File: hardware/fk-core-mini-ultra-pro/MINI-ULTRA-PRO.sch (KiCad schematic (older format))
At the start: 70 parts, among them J1 S2B-PH-SM4-TB, J2 MICRO-USB, J3 RF-SMA-EDGE, J4 CONN-HDR-1x19, J5 CONN-HDR-1x19, J6 CONN-HDR-2x5, J7 RF-SMA-EDGE, M1 MOUNT_HOLE, M2 MOUNT_HOLE, M3 MOUNT_HOLE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

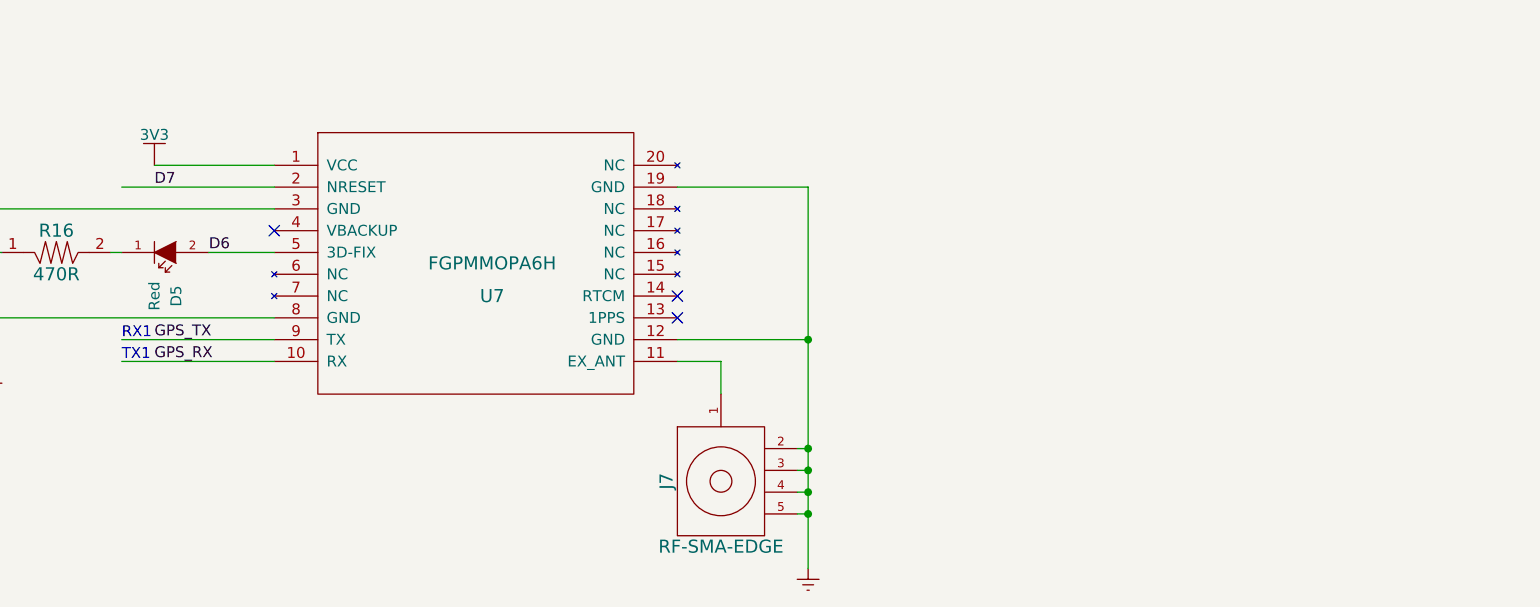
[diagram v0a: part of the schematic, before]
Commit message: Laying out our additions to the MUP pcb. SD/GPS/Fuel gauge.
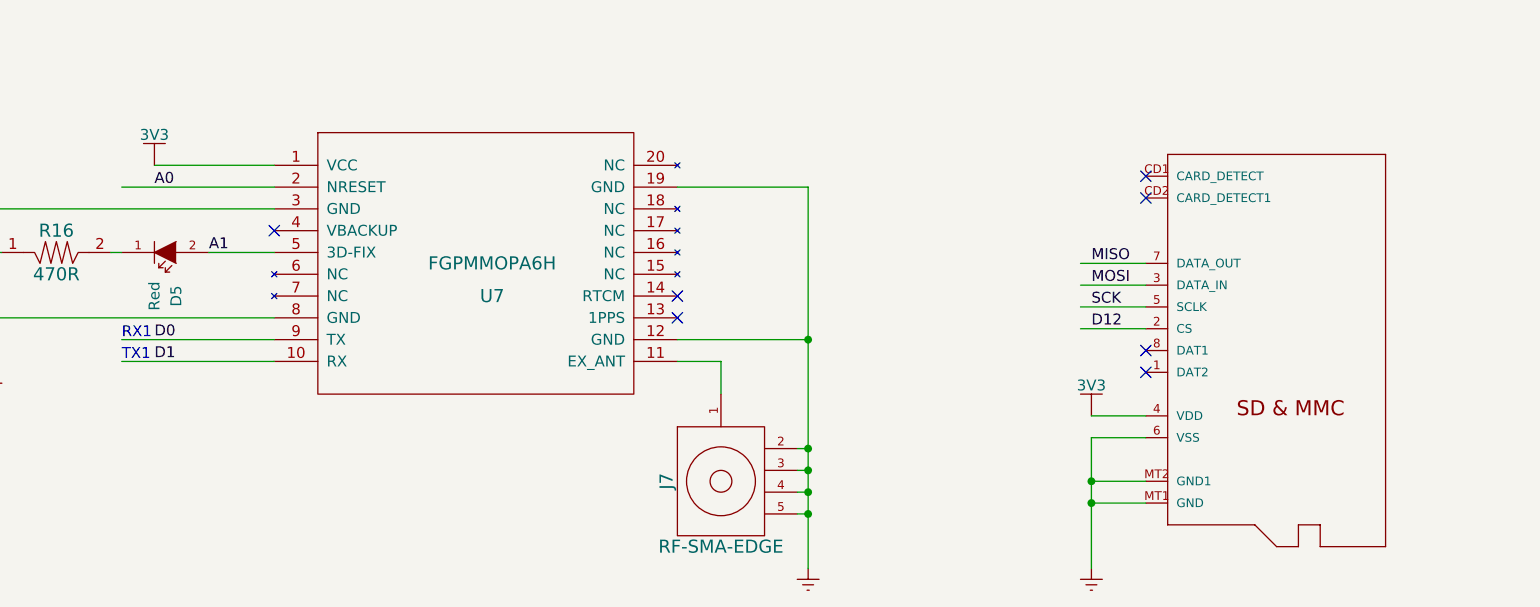
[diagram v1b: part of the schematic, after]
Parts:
- added M7: MICROSD, microsd:MICROSD, symbol MICROSD
- U7: footprint (none) -> FGPMMOPA6H:FGPMMOPA6H
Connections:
- net labels removed: GPS_RX, GPS_TX
- wire segments 317 -> 326
- no-connect marks 21 -> 25
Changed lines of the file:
@@
 F 0 "U7" H 8450 12350 60  0000 C CNN
 F 1 "FGPMMOPA6H" H 8450 12500 60  0000 C CNN
-F 2 "" H 8450 12500 60  0001 C CNN
+F 2 "FGPMMOPA6H:FGPMMOPA6H" H 8450 12500 60  0001 C CNN
 F 3 "" H 8450 12500 60  0001 C CNN
 	1    8450 12500
@@
 Connection ~ 6150 12450
 Text Label 6900 12150 0    50   ~ 0
-D7
+A0
 Text Label 6900 12850 0    50   ~ 0
-GPS_TX
+D0
 Text Label 6900 12950 0    50   ~ 0
-GPS_RX
+D1
 Text Label 7150 12450 0    50   ~ 0
-D6
+A1
 Text Notes 6750 12950 0    50   ~ 0
 TX1
 Text Notes 6750 12850 0    50   ~ 0
 RX1
+$Comp
+L MICROSD M7
+U 1 1 58837EB0
+P 12150 12800
+F 0 "M7" H 12150 12800 45  0001 C CNN
+F 1 "MICROSD" H 12150 12800 45  0001 C CNN
+F 2 "microsd:MICROSD" H 12180 12950 20  0001 C CNN
+F 3 "" H 12150 12800 60  0001 C CNN
+	1    12150 12800
+	1    0    0    -1
+$EndComp
+NoConn ~ 11450 12100
+NoConn ~ 11450 12200
+$Comp
+L GND #PWR070
+U 1 1 58838941
+P 11200 13900
+F 0 "#PWR070" H 11200 13650 50  0001 C CNN
+F 1 "GND" H 11200 13750 50  0001 C CNN
+F 2 "" H 11200 13900 60  0000 C CNN
+F 3 "" H 11200 13900 60  0000 C CNN
+	1    11200 13900
+	1    0    0    -1
+$EndComp
+Wire Wire Line
+	11450 13500 11200 13500
+Wire Wire Line
+	11200 13300 11200 13900
+Wire Wire Line
+	11450 13600 11200 13600
+Connection ~ 11200 13600
+Wire Wire Line
+	11450 13300 11200 13300
+Connection ~ 11200 13500
+$Comp
+L 3V3 #PWR071
+U 1 1 58839315
+P 11200 13200
+F 0 "#PWR071" H 11200 13050 50  0001 C CNN
+F 1 "3V3" H 11200 13340 50  0000 C CNN
+F 2 "" H 11200 13200 60  0000 C CNN
+F 3 "" H 11200 13200 60  0000 C CNN
+	1    11200 13200
+	1    0    0    -1
+$EndComp
+Wire Wire Line
+	11450 13200 11200 13200
+NoConn ~ 11450 12900
+NoConn ~ 11450 13000
+Text Label 11200 12600 0    50   ~ 0
+MOSI
+Text Label 11200 12500 0    50   ~ 0
+MISO
+Text Label 11200 12700 0    50   ~ 0
+SCK
+Wire Wire Line
+	11450 12700 11150 12700
+Wire Wire Line
+	11150 12600 11450 12600
+Wire Wire Line
+	11150 12500 11450 12500
+Wire Wire Line
+	11150 12800 11450 12800
+Text Label 11200 12800 0    50   ~ 0
+D12
 $EndSCHEMATC

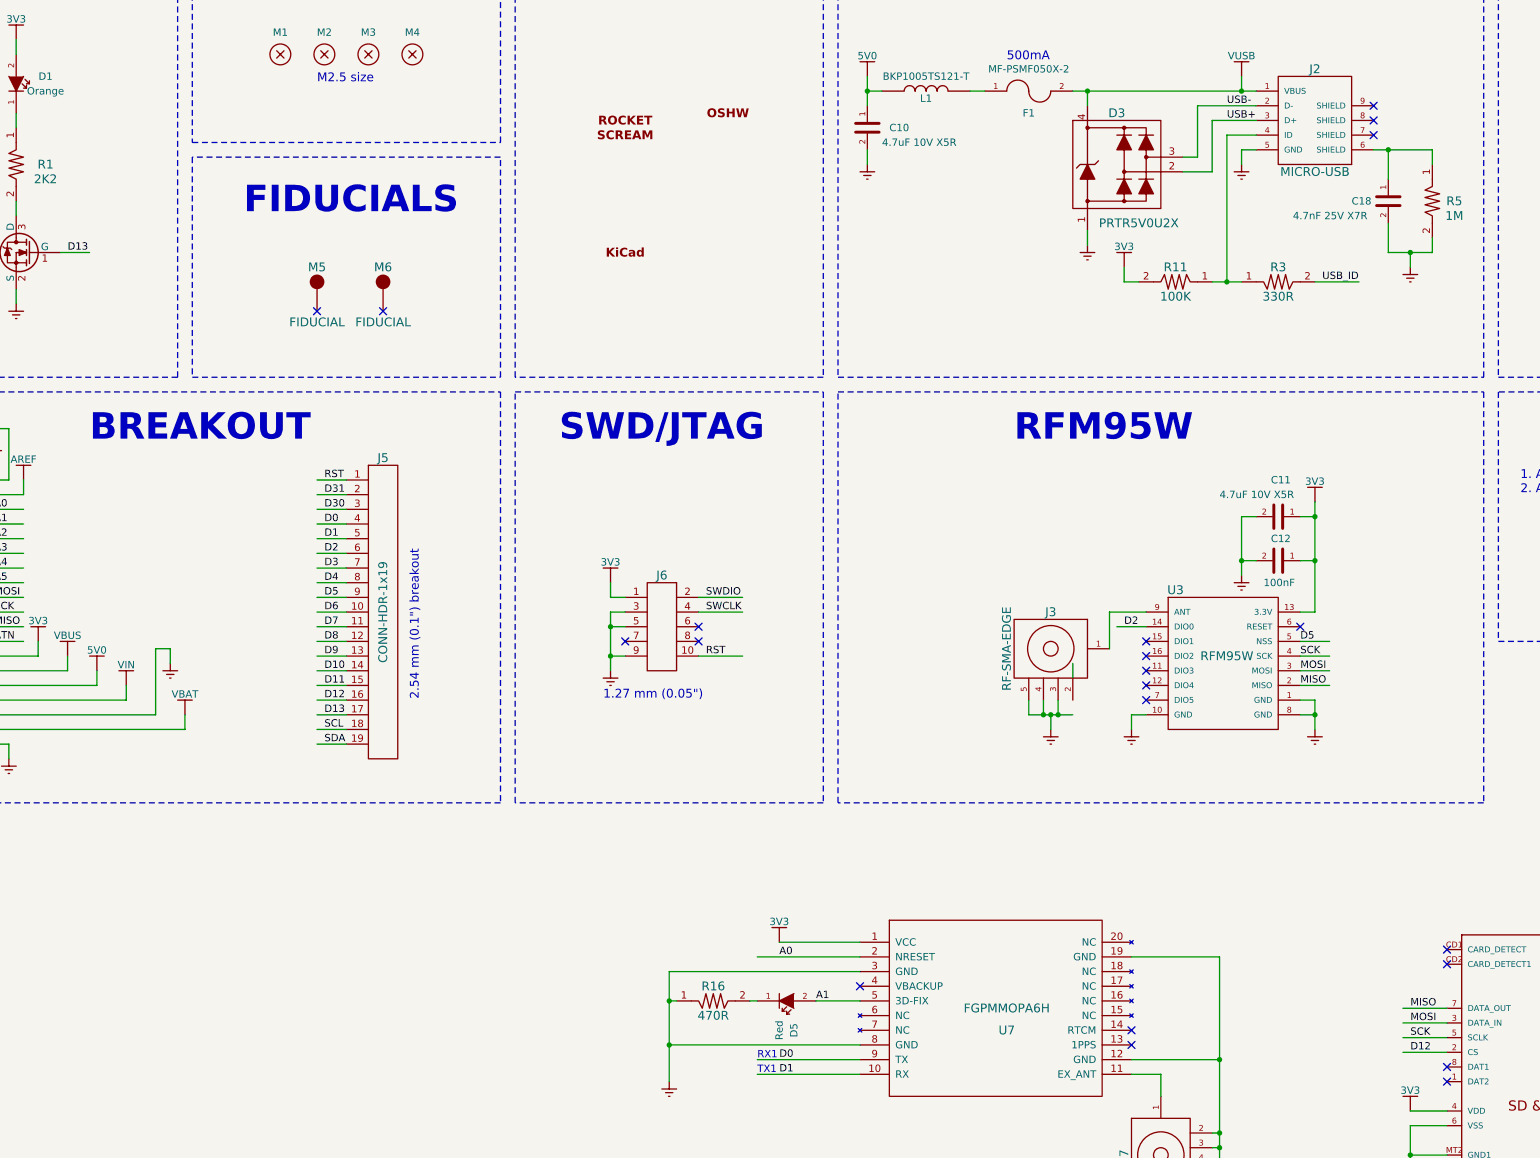
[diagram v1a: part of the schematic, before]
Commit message: Some layout tweaks, also adding a module header.
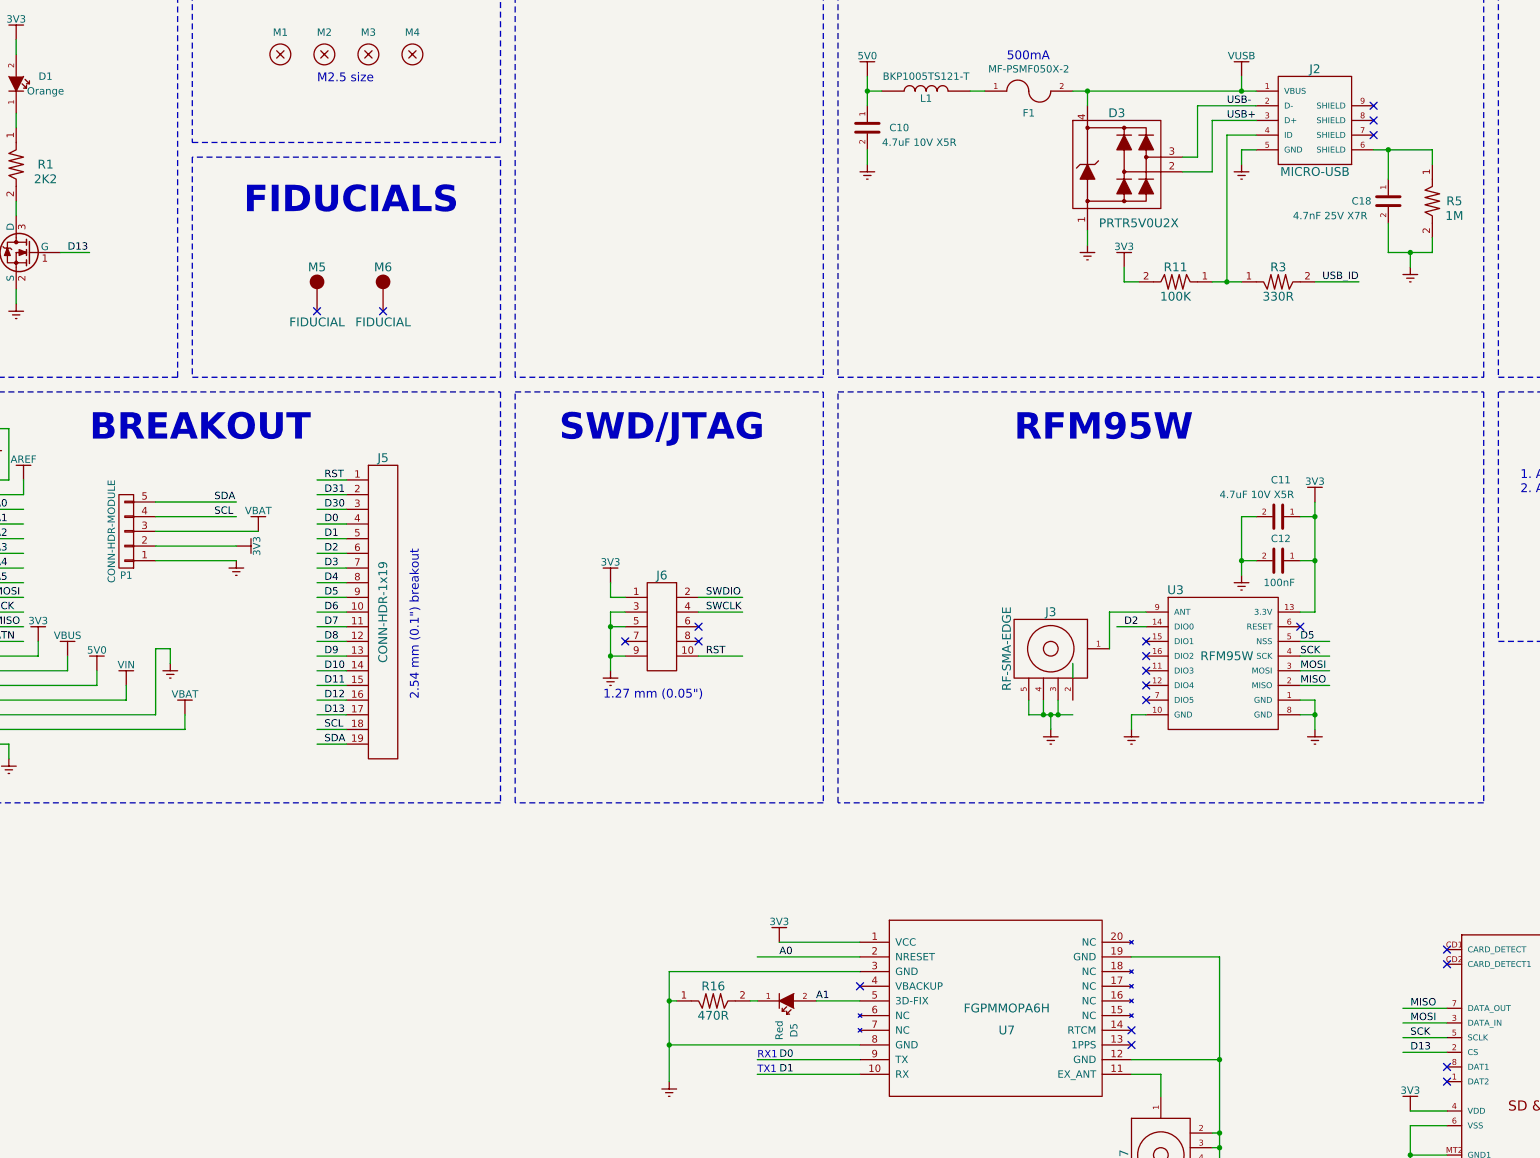
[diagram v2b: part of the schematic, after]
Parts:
- removed LOGO1: LOGO-ROCKET-SCREAM, RocketScreamKicadLibrary:LOGO-ROCKET-SCREAM_Vertical_Small, symbol LOGO-ROCKET-SCREAM
- removed LOGO2: LOGO-OSHW, RocketScreamKicadLibrary:LOGO-OSHW_Small, symbol LOGO-OSHW
- removed LOGO3: LOGO-KICAD, RocketScreamKicadLibrary:LOGO-KICAD_XSmall, symbol LOGO-KICAD
- added P1: CONN-HDR-MODULE, fk-core-mini-ultra-pro:Socket_Strip_Straight_1x05_Pitch2.54mm, symbol CONN_01X05
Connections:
- wire segments 326 -> 331

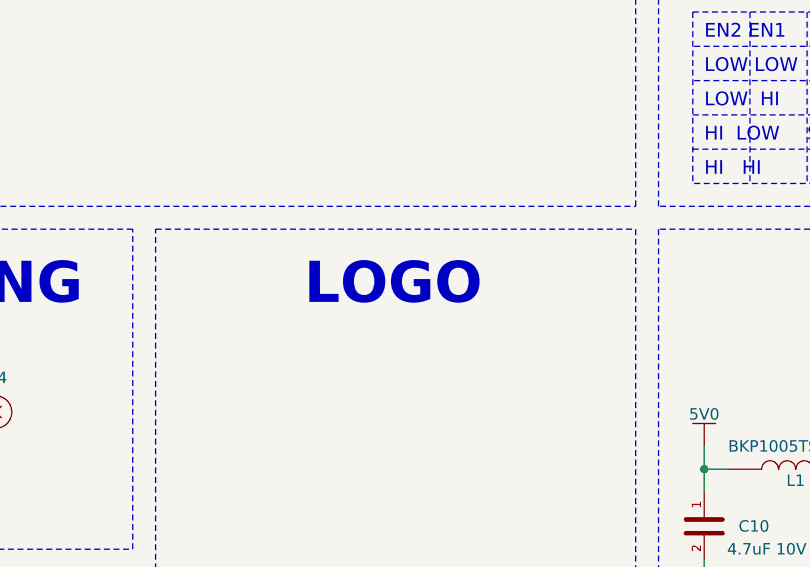
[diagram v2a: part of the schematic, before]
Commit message: Adding header for modules to PCB.
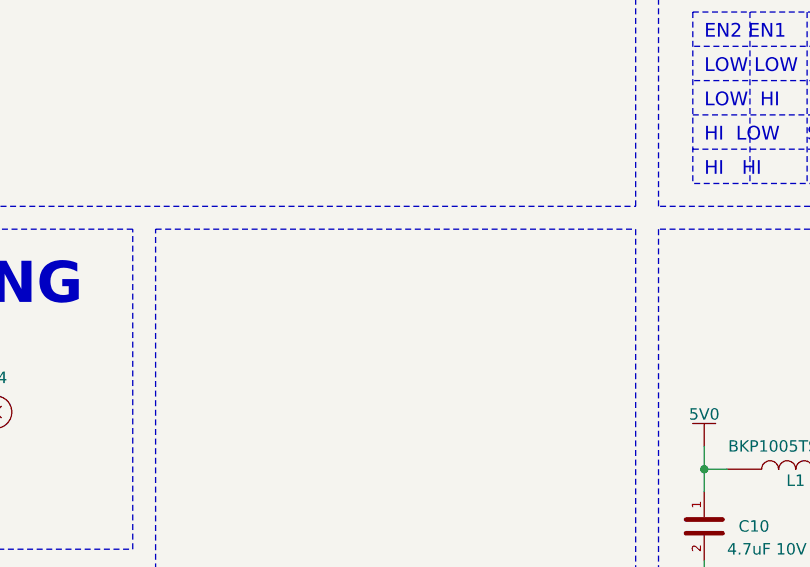
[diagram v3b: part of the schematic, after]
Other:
- note removed: "LOGO"
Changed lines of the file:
@@
 LIBS:max1704xx
 LIBS:conn_01x05
+LIBS:ws2812
 EELAYER 25 0
 EELAYER END
@@
 Wire Notes Line
 	15900 8300 11800 8300
-Text Notes 5750 5550 0    180  ~ 36
-LOGO
 Text Notes 3250 5550 0    180  ~ 36
 MOUNTING

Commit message: Pull ups on SDA/SCL and some tweaks.
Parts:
- added R17, R18: 4.7K, RocketScreamKicadLibrary:RES-0603, symbol RESISTOR
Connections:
- net labels added: SD_CS
- wire segments 331 -> 335
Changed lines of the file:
@@
 	2850 3700 2550 3700
-Wire Wire Line
-	2850 3800 2550 3800
 Wire Wire Line
 	2850 3900 2550 3900
@@
 Text Label 2550 3700 0    50   ~ 0
 D11
-Text Label 2550 3800 0    50   ~ 0
-D13
 Text Label 2550 3900 0    50   ~ 0
 D10
@@
 	3750 10400 3950 10400
 Wire Wire Line
-	3750 10500 3950 10500
+	3450 10500 3950 10500
 Wire Wire Line
 	3750 10600 3950 10600
@@
 	11150 12800 11450 12800
 Text Label 11200 12800 0    50   ~ 0
-D13
+SD_CS
 $Comp
 L CONN_01X05 P1
@@
 	1    0    0    -1
 $EndComp
+Text Label 10950 4250 0    50   ~ 0
+SDA
+Text Label 10950 4650 0    50   ~ 0
+SCL
+$Comp
+L RESISTOR R17
+U 1 1 58BACE90
+P 11400 4250
+F 0 "R17" H 11300 4100 60  0000 C CNN
+F 1 "4.7K" H 11500 4100 60  0000 C CNN
+F 2 "RocketScreamKicadLibrary:RES-0603" H 11400 4050 60  0001 C CNN
+F 3 "" H 11400 4250 60  0000 C CNN
+	1    11400 4250
+	-1   0    0    1
+$EndComp
+$Comp
+L RESISTOR R18
+U 1 1 58BAD0B7
+P 11400 4650
+F 0 "R18" H 11300 4500 60  0000 C CNN
+F 1 "4.7K" H 11500 4500 60  0000 C CNN
+F 2 "RocketScreamKicadLibrary:RES-0603" H 11400 4450 60  0001 C CNN
+F 3 "" H 11400 4650 60  0000 C CNN
+	1    11400 4650
+	-1   0    0    1
+$EndComp
+Wire Wire Line
+	11150 4650 10950 4650
+Wire Wire Line
+	10950 4250 11150 4250
+$Comp
+L 3V3 #PWR075
+U 1 1 58BADC48
+P 11750 4250
+F 0 "#PWR075" H 11750 4100 50  0001 C CNN
+F 1 "3V3" H 11750 4390 50  0000 C CNN
+F 2 "" H 11750 4250 60  0000 C CNN
+F 3 "" H 11750 4250 60  0000 C CNN
+	1    11750 4250
+	1    0    0    -1
+$EndComp
+Wire Wire Line
+	11750 4250 11650 4250
+$Comp
+L 3V3 #PWR076
+U 1 1 58BADF2B
+P 11750 4650
+F 0 "#PWR076" H 11750 4500 50  0001 C CNN
+F 1 "3V3" H 11750 4790 50  0000 C CNN
+F 2 "" H 11750 4650 60  0000 C CNN
+F 3 "" H 11750 4650 60  0000 C CNN
+	1    11750 4650
+	1    0    0    -1
+$EndComp
+Wire Wire Line
+	11750 4650 11650 4650
+Text Label 2550 3800 0    50   ~ 0
+SD_CS
+Wire Wire Line
+	2550 3800 2850 3800
+Text Label 3450 10500 0    50   ~ 0
+SD_CS
 $EndSCHEMATC
